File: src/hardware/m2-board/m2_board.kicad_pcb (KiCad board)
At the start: 2 copper layers, 60 x 40 mm, 17 parts, among them J1 TYPE-C-31-M-12, SW1 TS-1088R-02026, SW2 TS-1088R-02026, U1 ESP32-C3-WROOM-02-N4, U2 SHT30-DIS-B10KS, U3 ME6211C33M5G-N

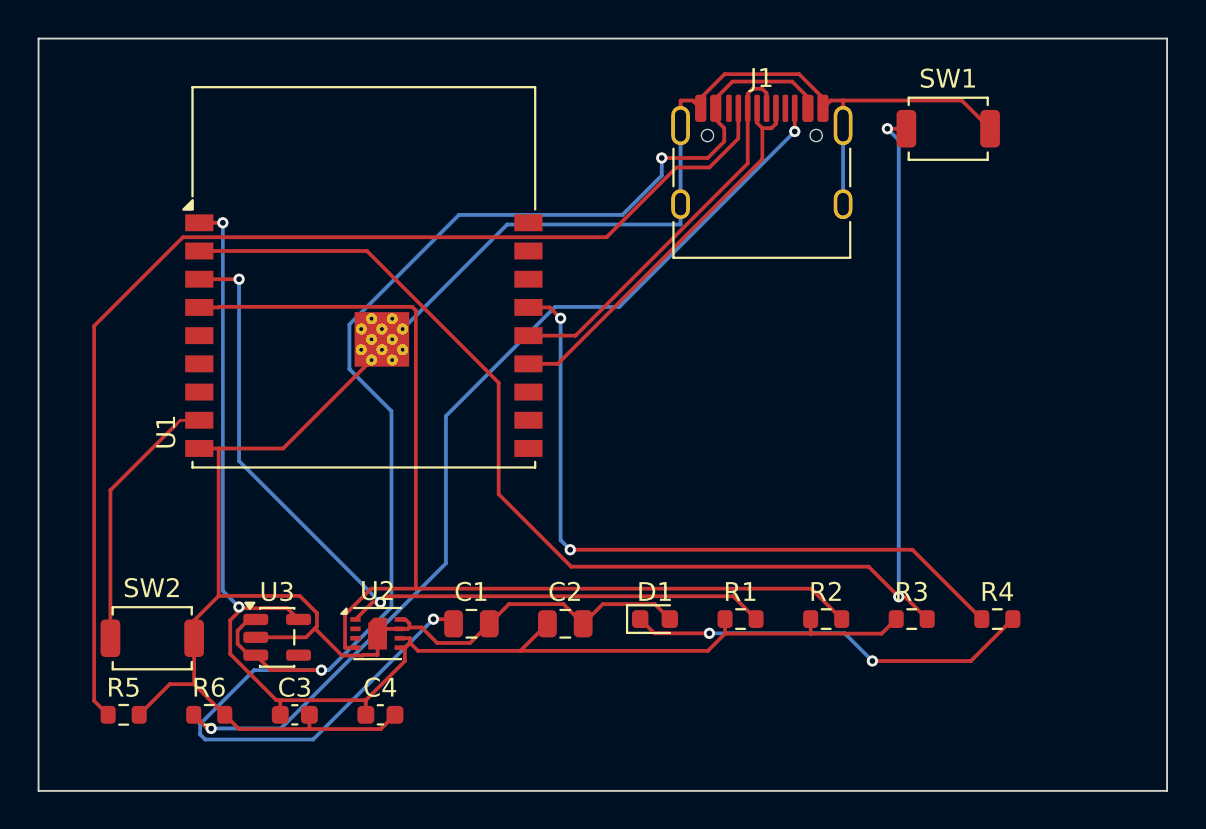
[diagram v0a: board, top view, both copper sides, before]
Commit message: feat: close M2 board review with signed manufacturing release
- Rebuild PCB with functional placement (J1 edge-mounted, decoupling
  caps next to ICs, SHT30 thermally isolated) and hand-fanned USB-C
  tongue escape (0.4/0.2mm vias for the 0.5mm-pitch corridor)
- Converge DRC from 5 violations to zero: min via 0.4mm rule, CC2 via
  relocation (clearance 0.10->0.48mm), USB_DM B.Cu direct tie,
  dangling via removal, 0.55mm serpentine (skew 1.97->0.87mm)
- Add tools/board_review.py: 8-item machine-measured review, all PASS
  (USB edge 0.03mm, antenna keepout clear, decoupling 2.8mm worst,
  thermal 35.2mm, silk 17/17)
- Sign gates/board_review_v1.json manufacturing_release=true (named
  reviewer, ISO timestamp, per-item measured evidence)
- Regenerate delivery from current board (gerbers/drill/pos, 26-entry
  ZIP) and refresh ERC/DRC/manifest evidence; re-render board images
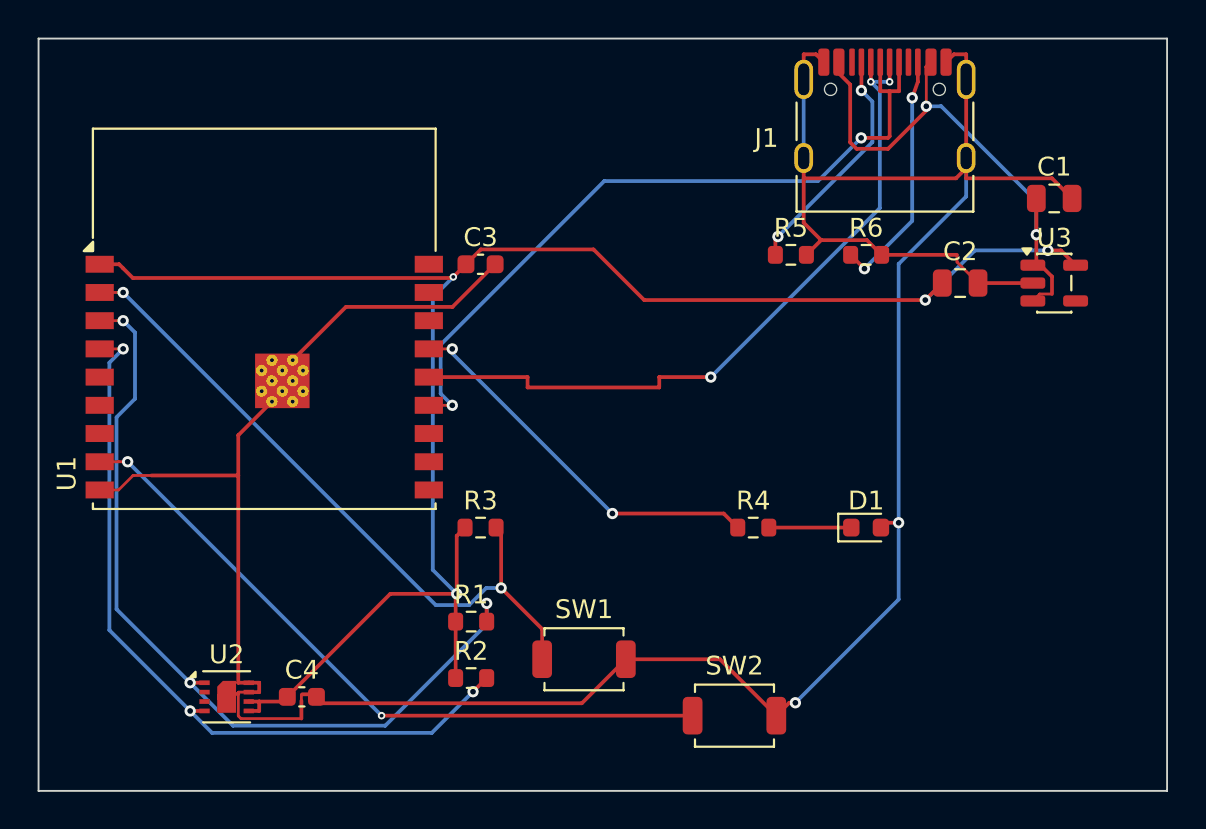
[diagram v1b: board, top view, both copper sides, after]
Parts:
- moved U3 45.4 mm to (54.0, 13.0)
- moved R5 43.1 mm to (40.0, 11.5)
- moved R6 42.6 mm to (44.0, 11.5)
- moved C1 38.4 mm to (54.0, 8.50)
- moved SW1 34.2 mm to (29.0, 33.0)
- moved SW2 31.2 mm to (37.0, 36.0)
- moved C2 27.7 mm to (49.0, 13.0)
- moved C3 25.9 mm to (23.5, 12.0)
- moved R3 23.4 mm to (23.5, 26.0)
- moved R2 19.1 mm to (23.0, 34.0)
- moved R1 14.3 mm to (23.0, 31.0)
- moved R4 13.9 mm to (38.0, 26.0)
- moved D1 12.2 mm to (44.0, 26.0)
- moved U2 8.70 mm to (10.0, 35.0)
- moved J1 6.99 mm to (45.0, 5.30)
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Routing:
- net +5V: track 85.7 -> 28.9 mm, vias 3 -> 2
- net CC1: track 61.0 -> 12.6 mm, vias 0 -> 2
- net EN: track 76.4 -> 36.6 mm
- net CC2: track 51.2 -> 13.1 mm
- net GND: track 132.2 -> 165.1 mm, vias 0 -> 2
- net +3V3: track 73.3 -> 97.2 mm, vias 2 -> 4
- net BOOT: track 14.1 -> 37.1 mm, vias 0 -> 2
- net USB_DP: track 21.4 -> 39.7 mm, vias 0 -> 2
- net USB_DM: track 21.2 -> 38.8 mm, vias 0 -> 3
- net LED_DRV: track 37.9 -> 20.5 mm
- net LED_A: track 21.7 -> 4.39 mm, vias 2 -> 0
- net SCL: track 56.4 -> 40.8 mm, vias 0 -> 3
- net SDA: track 44.7 -> 44.6 mm, vias 2 -> 3

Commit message: fix(pcb): reconcile M2 semantics and routing [AI-20260830-001]
- add and route R7/R8/R9/C5 with corrected USB and SHT30 topology
- verify full USB channel identities and length skew across series resistors
- converge KiCad DRC to 0 violations and 0 unconnected while release remains revoked
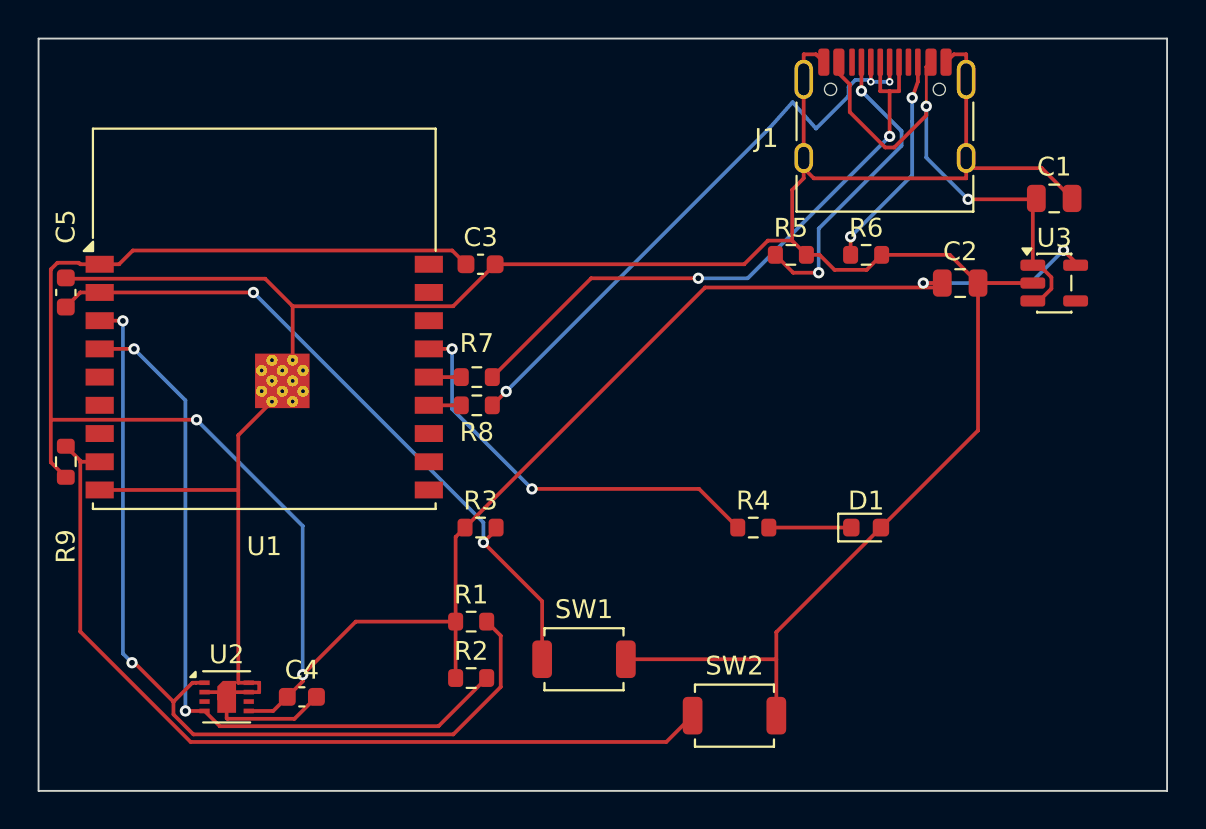
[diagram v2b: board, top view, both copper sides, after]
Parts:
- added C5: 1uF, C_0603_1608Metric, F.Cu at (1.45, 13.5)
- added R7: 22R, R_0603_1608Metric, F.Cu at (23.3, 18.0)
- added R8: 22R, R_0603_1608Metric, F.Cu at (23.3, 19.5)
- added R9: 10k, R_0603_1608Metric, F.Cu at (1.45, 22.5)
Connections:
- J1 pad A6: USB_DP -> USB_DP_CONN
- J1 pad A7: USB_DM -> USB_DM_CONN
- J1 pad B6: USB_DP -> USB_DP_CONN
- J1 pad B7: USB_DM -> USB_DM_CONN
- U1 pad 13: USB_DP -> USB_DM
- U1 pad 14: USB_DM -> USB_DP
- U2 pad 2: (no net) -> GND
- U2 pad 6: +3V3 -> (no net)
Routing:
- net USB_DP: track 39.7 -> 1.73 mm, vias 2 -> 0
- net USB_DM: track 38.8 -> 1.73 mm, vias 3 -> 0
- net USB_DP_CONN: track 0.00 -> 32.9 mm, vias 0 -> 2
- net USB_DM_CONN: track 0.00 -> 32.0 mm, vias 0 -> 3
- net +3V3: track 97.2 -> 120.3 mm
- net BOOT: track 37.1 -> 46.8 mm, vias 2 -> 0
- net GND: track 165.1 -> 170.9 mm, vias 2 -> 0
- net CC1: track 12.6 -> 16.6 mm
- net SDA: track 44.6 -> 48.1 mm, vias 3 -> 2
- net LED_DRV: track 20.5 -> 22.2 mm
- net CC2: track 13.1 -> 11.7 mm
- net +5V: track 28.9 -> 27.5 mm
- net SCL: track 40.8 -> 39.6 mm, vias 3 -> 2
- net EN: track 36.6 -> 37.2 mm

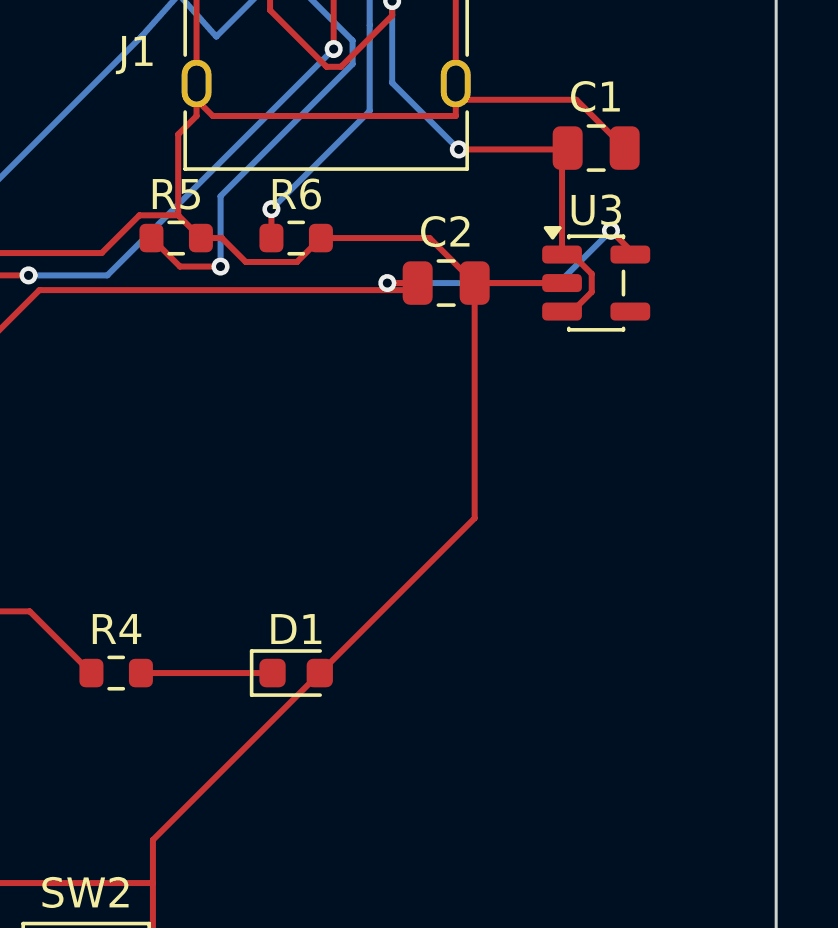
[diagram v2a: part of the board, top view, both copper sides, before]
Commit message: fix(board): repair D1 LED polarity and swap U3 to C235316 [AI-20260831-007]
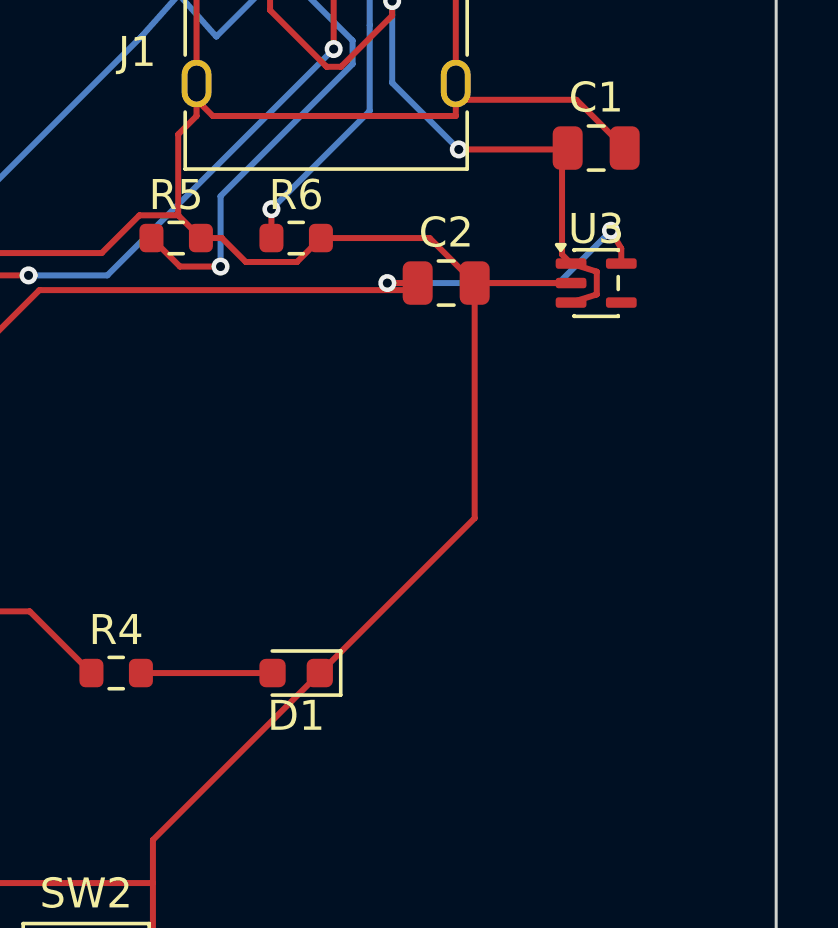
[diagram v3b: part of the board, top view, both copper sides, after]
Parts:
- U3: value ME6211C33M5G-N -> ME6211C33R5G; footprint SOT-23-5 -> SOT-353_SC-70-5
- turned D1 to 180 degrees
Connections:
- D1 pad 1: LED_A -> GND
- D1 pad 2: GND -> LED_A
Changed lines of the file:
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@@
 		)
 	)
-	(footprint "SOT-23-5"
+	(footprint "SOT-353_SC-70-5"
 		(layer "F.Cu")
 		(at 54 13)
-		(descr "SOT, 5 Pin (JEDEC MO-178 Var AA https://www.jedec.org/document_search?search_api_views_fulltext=MO-178)")
-		(tags "SOT TO_SOT_SMD")
+		(descr "SOT, 5 Pin (https://home.jeita.or.jp/tsc/std-pdf/ED-7500A.pdf#page=171, JEDEC MO-203, variant AA, https://www.jedec.org/document_search?search_api_views_fulltext=MO-203)")
+		(tags "SOT TO_SOT_SMD SC-88A SOT-353 SC-70-5")
 		(property "Reference" "U3"
-			(at 0 -2.4 0)
+			(at 0 -1.8 0)
 			(layer "F.SilkS")
 			(effects
@@
 			)
 		)
-		(property "Value" "ME6211C33M5G-N"
-			(at 0 2.4 0)
+		(property "Value" "ME6211C33R5G"
+			(at 0 1.8 0)
 			(layer "F.Fab")
 			(effects
@@
 		(duplicate_pad_numbers_are_jumpers no)
 		(fp_line
-			(start -0.91 -1.56)
-			(end 0.91 -1.56)
+			(start -0.735 -1.11)
+			(end 0.735 -1.11)
 			(stroke
 				(width 0.12)
@@
 		)
 		(fp_line
-			(start -0.91 -1.51)
-			(end -0.91 -1.56)
+			(start -0.735 -1.085)
+			(end -0.735 -1.11)
 			(stroke
 				(width 0.12)
@@
 		)
 		(fp_line
-			(start -0.91 1.56)
-			(end -0.91 1.51)
+			(start -0.735 1.11)
+			(end -0.735 1.085)
 			(stroke
 				(width 0.12)
@@
 		)
 		(fp_line
-			(start 0.91 -1.56)
-			(end 0.91 -1.51)
+			(start 0.735 -1.11)
+			(end 0.735 -1.085)
 			(stroke
 				(width 0.12)
@@
 		)
 		(fp_line
-			(start 0.91 -0.39)
-			(end 0.91 0.39)
+			(start 0.735 -0.215)
+			(end 0.735 0.215)
 			(stroke
 				(width 0.12)
@@
 		)
 		(fp_line
-			(start 0.91 1.51)
-			(end 0.91 1.56)
+			(start 0.735 1.085)
+			(end 0.735 1.11)
 			(stroke
 				(width 0.12)
@@
 		)
 		(fp_line
-			(start 0.91 1.56)
-			(end -0.91 1.56)
+			(start 0.735 1.11)
+			(end -0.735 1.11)
 			(stroke
 				(width 0.12)
@@
 		(fp_poly
 			(pts
-				(xy -1.45 -1.51) (xy -1.69 -1.84) (xy -1.21 -1.84)
+				(xy -1.18 -1.09) (xy -1.32 -1.28) (xy -1.04 -1.28)
 			)
 			(stroke
@@
 		)
 		(fp_line
-			(start -2.05 -1.5)
-			(end -1.05 -1.5)
+			(start -1.45 -0.93)
+			(end -0.73 -0.93)
 			(stroke
 				(width 0.05)
@@
 		)
 		(fp_line
-			(start -2.05 1.5)
-			(end -2.05 -1.5)
+			(start -1.45 0.93)
+			(end -1.45 -0.93)
 			(stroke
 				(width 0.05)
@@
 		)
 		(fp_line
-			(start -1.05 -1.7)
-			(end 1.05 -1.7)
+			(start -0.73 -1.1)
+			(end 0.73 -1.1)
 			(stroke
 				(width 0.05)
@@
 		)
 		(fp_line
-			(start -1.05 -1.5)
-			(end -1.05 -1.7)
+			(start -0.73 -0.93)
+			(end -0.73 -1.1)
 			(stroke
 				(width 0.05)
@@
 		)
 		(fp_line
-			(start -1.05 1.5)
-			(end -2.05 1.5)
+			(start -0.73 0.93)
+			(end -1.45 0.93)
 			(stroke
 				(width 0.05)
@@
 		)
 		(fp_line
-			(start -1.05 1.7)
-			(end -1.05 1.5)
+			(start -0.73 1.1)
+			(end -0.73 0.93)
 			(stroke
 				(width 0.05)
@@
 		)
 		(fp_line
-			(start 1.05 -1.7)
-			(end 1.05 -1.5)
+			(start 0.73 -1.1)
+			(end 0.73 -0.93)
 			(stroke
 				(width 0.05)
@@
 		)
 		(fp_line
-			(start 1.05 -1.5)
-			(end 2.05 -1.5)
+			(start 0.73 -0.93)
+			(end 1.45 -0.93)
 			(stroke
 				(width 0.05)
@@
 		)
 		(fp_line
-			(start 1.05 -0.39)
-			(end 1.05 0.39)
+			(start 0.73 -0.37)
+			(end 0.73 0.37)
 			(stroke
 				(width 0.05)
@@
 		)
 		(fp_line
-			(start 1.05 0.39)
-			(end 2.05 0.39)
+			(start 0.73 0.37)
+			(end 1.45 0.37)
 			(stroke
 				(width 0.05)
@@
 		)
 		(fp_line
-			(start 1.05 1.5)
-			(end 1.05 1.7)
+			(start 0.73 0.93)
+			(end 0.73 1.1)
 			(stroke
 				(width 0.05)
@@
 		)
 		(fp_line
-			(start 1.05 1.7)
-			(end -1.05 1.7)
+			(start 0.73 1.1)
+			(end -0.73 1.1)
 			(stroke
 				(width 0.05)
@@
 		)
 		(fp_line
-			(start 2.05 -1.5)
-			(end 2.05 -0.39)
+			(start 1.45 -0.93)
+			(end 1.45 -0.37)
 			(stroke
 				(width 0.05)
@@
 		)
 		(fp_line
-			(start 2.05 -0.39)
-			(end 1.05 -0.39)
+			(start 1.45 -0.37)
+			(end 0.73 -0.37)
 			(stroke
 				(width 0.05)
@@
 		)
 		(fp_line
-			(start 2.05 0.39)
-			(end 2.05 1.5)
+			(start 1.45 0.37)
+			(end 1.45 0.93)
 			(stroke
 				(width 0.05)
@@
 		)
 		(fp_line
-			(start 2.05 1.5)
-			(end 1.05 1.5)
+			(start 1.45 0.93)
+			(end 0.73 0.93)
 			(stroke
 				(width 0.05)
@@
 		(fp_poly
 			(pts
-				(xy -0.4 -1.45) (xy 0.8 -1.45) (xy 0.8 1.45) (xy -0.8 1.45) (xy -0.8 -1.05)
+				(xy -0.3125 -1) (xy 0.625 -1) (xy 0.625 1) (xy -0.625 1) (xy -0.625 -0.6875)
 			)
 			(stroke
@@
 			(effects
 				(font
-					(size 0.72 0.72)
-					(thickness 0.11)
+					(size 0.5 0.5)
+					(thickness 0.08)
 				)
 			)
 		)
 		(pad "1" smd roundrect
-			(at -1.1375 -0.95)
-			(size 1.325 0.6)
+			(at -0.8375 -0.65)
+			(size 1.025 0.35)
 			(layers "F.Cu" "F.Mask" "F.Paste")
 			(roundrect_rratio 0.25)
@@
 		)
 		(pad "2" smd roundrect
-			(at -1.1375 0)
-			(size 1.325 0.6)
+			(at -0.8375 0)
+			(size 1.025 0.35)
 			(layers "F.Cu" "F.Mask" "F.Paste")
 			(roundrect_rratio 0.25)
@@
 		)
 		(pad "3" smd roundrect
-			(at -1.1375 0.95)
-			(size 1.325 0.6)
+			(at -0.8375 0.65)
+			(size 1.025 0.35)
 			(layers "F.Cu" "F.Mask" "F.Paste")
 			(roundrect_rratio 0.25)
@@
 		)
 		(pad "4" smd roundrect
-			(at 1.1375 0.95)
-			(size 1.325 0.6)
+			(at 0.8375 0.65)
+			(size 1.025 0.35)
 			(layers "F.Cu" "F.Mask" "F.Paste")
 			(roundrect_rratio 0.25)
 		)
 		(pad "5" smd roundrect
-			(at 1.1375 -0.95)
-			(size 1.325 0.6)
+			(at 0.8375 -0.65)
+			(size 1.025 0.35)
 			(layers "F.Cu" "F.Mask" "F.Paste")
 			(roundrect_rratio 0.25)
@@
 		)
 		(embedded_fonts no)
-		(model "${KICAD10_3DMODEL_DIR}/Package_TO_SOT_SMD.3dshapes/SOT-23-5.step"
+		(model "${KICAD10_3DMODEL_DIR}/Package_TO_SOT_SMD.3dshapes/SOT-353_SC-70-5.step"
 			(offset
 				(xyz 0 0 0)
@@
 	(footprint "LED_0603_1608Metric"
 		(layer "F.Cu")
-		(at 44 26)
+		(at 44 26 180)
 		(descr "LED SMD 0603 (1608 Metric), square (rectangular) end terminal, IPC-7351 nominal, (Body size source: http://www.tortai-tech.com/upload/download/2011102023233369053.pdf)")
 		(tags "LED")
@@
 			(layers "F.Cu" "F.Mask" "F.Paste")
 			(roundrect_rratio 0.25)
-			(net "LED_A")
+			(net "GND")
 		)
 		(pad "2" smd roundrect
@@
 			(layers "F.Cu" "F.Mask" "F.Paste")
 			(roundrect_rratio 0.25)
-			(net "GND")
+			(net "LED_A")
 		)
 		(embedded_fonts no)
@@
 	)
 	(segment
-		(start 55.1375 11.9015)
-		(end 55.1375 12.05)
+		(start 54.8375 11.85)
+		(end 54.8375 12.35)
 		(width 0.2)
 		(layer "F.Cu")
@@
 	(segment
 		(start 54.493 11.257)
-		(end 55.1375 11.9015)
+		(end 54.8375 11.85)
 		(width 0.2)
 		(layer "F.Cu")
@@
 	)
 	(segment
-		(start 52.8625 13.95)
-		(end 53.201 13.95)
-		(width 0.2)
-		(layer "F.Cu")
-		(net "+5V")
-	)
-	(segment
 		(start 47.2 4.0851)
 		(end 45.4933 5.7918)
@@
 	)
 	(segment
-		(start 53.201 13.95)
-		(end 53.8521 13.2989)
+		(start 54.02 13.38)
+		(end 53.1625 13.65)
 		(width 0.2)
 		(layer "F.Cu")
@@
 	)
 	(segment
-		(start 53.2065 12.05)
-		(end 52.8625 12.05)
+		(start 52.8625 12.05)
+		(end 53.1625 12.35)
 		(width 0.2)
 		(layer "F.Cu")
@@
 	)
 	(segment
-		(start 53.8521 13.2989)
-		(end 53.8521 12.6956)
+		(start 54.02 13.38)
+		(end 54.02 12.62)
 		(width 0.2)
 		(layer "F.Cu")
@@
 	)
 	(segment
-		(start 53.8521 12.6956)
-		(end 53.2065 12.05)
+		(start 53.1625 12.35)
+		(end 54.02 12.62)
 		(width 0.2)
 		(layer "F.Cu")
